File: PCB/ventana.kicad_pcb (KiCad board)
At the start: 2 copper layers, 78 x 49 mm, 55 parts, among them J1 Prog, J10 CLS, J2 SW1, J3 GND, J4 SW2, J5 GND, J6 VBat, J7 Motor+, J8 Motor-, J9 GND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

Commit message: Schematic and PCB
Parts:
- added C10: .01, Capacitor_SMD:C_1206_3216Metric, F.Cu at (105.8, 68.5)
- added C11: .01, Capacitor_SMD:C_1206_3216Metric, F.Cu at (105.8, 71.7)
- added D6: BZV55-B5V1.115, Diode_SMD:D_SOD-123, F.Cu at (100.2, 68.5)
- added D7: BZV55-B5V1.115, Diode_SMD:D_SOD-123, F.Cu at (100.2, 71.8)
- added R22: R, Resistor_SMD:R_1206_3216Metric, F.Cu at (111.5, 68.5)
- added R23: R, Resistor_SMD:R_1206_3216Metric, F.Cu at (111.5, 71.7)
- R21: value R47 -> 470

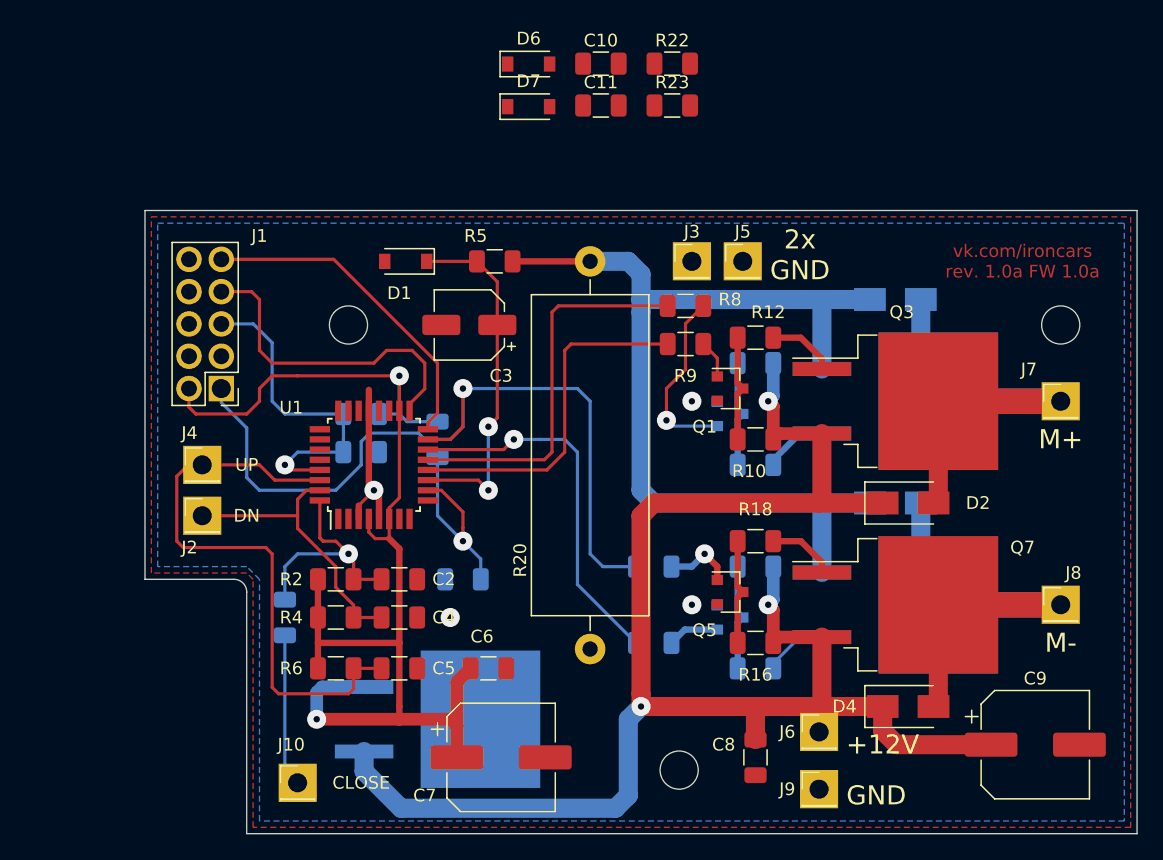
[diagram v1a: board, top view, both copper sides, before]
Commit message: Added parts for midpoints voltage measurement
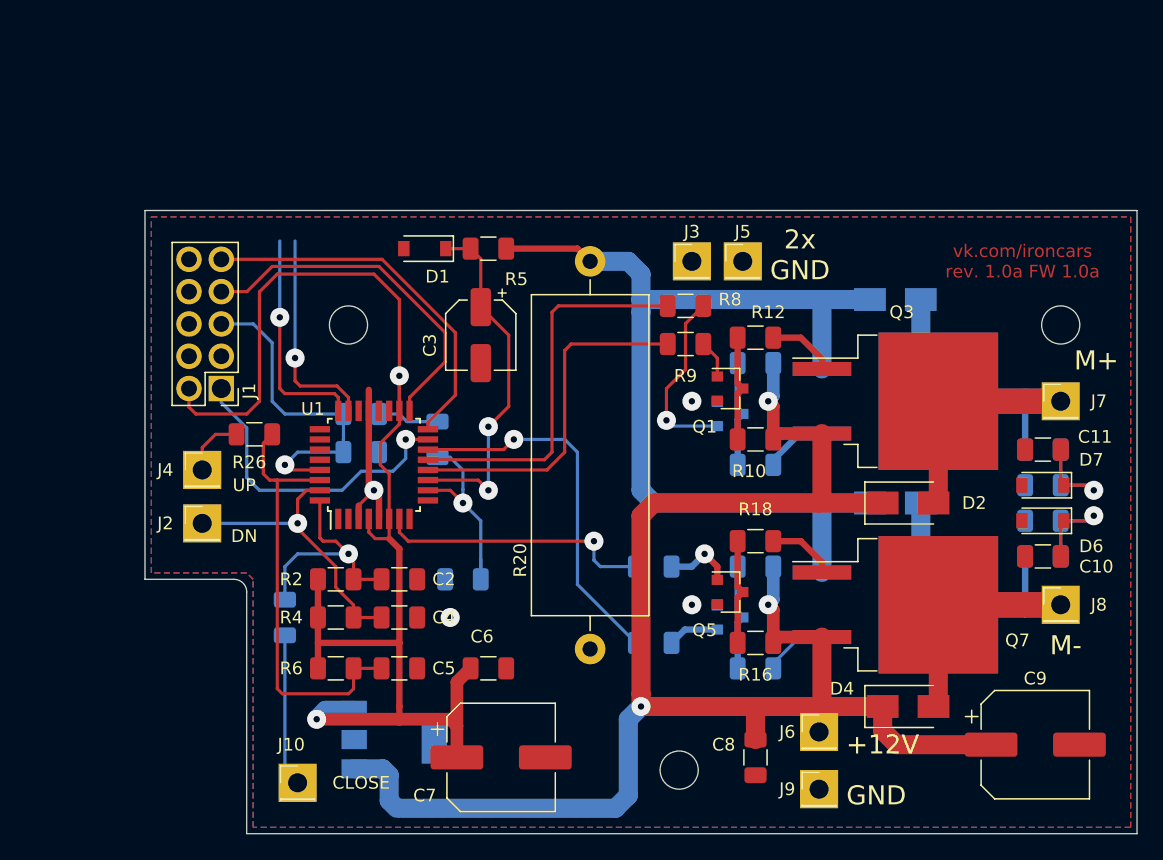
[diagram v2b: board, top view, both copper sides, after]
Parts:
- added R24: R, Resistor_SMD:R_1206_3216Metric, B.Cu at (140.6, 101.6)
- added R25: R, Resistor_SMD:R_1206_3216Metric, B.Cu at (140.6, 104.4)
- added R26: R, Resistor_SMD:R_1206_3216Metric, F.Cu at (78.6, 97.6)
- R22, R23: moved to B.Cu
- U2: value LM7805 -> LM2937; footprint Package_TO_SOT_SMD:TO-263-2 -> Package_TO_SOT_SMD:SOT-223
- moved D6 54.1 mm to (140.6, 104.4), turned to 180 degrees
- moved C10 52.0 mm to (140.6, 107.2)
- moved D7 50.2 mm to (140.6, 101.6), turned to 180 degrees
- moved R23 45.9 mm to (140.6, 107.2)
- moved C11 44.0 mm to (140.6, 98.8)
- moved R22 42.1 mm to (140.6, 98.8)
- moved U2 3.76 mm to (89.6, 121.6)
- moved D1 1.80 mm to (92.0, 83.0)
- moved C3 1.20 mm to (96.4, 89.8), turned to 270 degrees
- moved R5 1.12 mm to (97.0, 83.0)
- moved J2 0.60 mm to (74.5, 104.6)
- moved J4 0.40 mm to (74.5, 100.4)
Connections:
- J4 pad 1: Net-(C5-Pad1) -> Net-(J4-Pad1)
- R15 pad 2: Net-(J1-Pad1) -> Net-(R15-Pad2)
- R23 pad 1: Net-(D2-Pad2) -> Net-(D4-Pad2)
- U1 pad 7: Net-(U1-Pad7) -> Net-(R15-Pad2)
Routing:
- net Net-(J1-Pad1): track 64.4 -> 25.0 mm
- net Net-(C10-Pad2): track 0.00 -> 28.5 mm, vias 0 -> 2
- net Net-(C11-Pad2): track 0.00 -> 27.8 mm, vias 0 -> 2
- net Net-(R15-Pad2): track 0.00 -> 21.6 mm, vias 0 -> 1
- net Net-(C6-Pad1): track 96.5 -> 108.9 mm
- net Net-(C5-Pad1): track 46.2 -> 34.6 mm
- net Net-(J4-Pad1): track 0.00 -> 4.88 mm
- net Net-(D4-Pad2): track 36.0 -> 39.8 mm
- net Net-(D2-Pad2): track 36.0 -> 39.8 mm
- net Net-(J1-Pad9): track 25.9 -> 29.3 mm
- net Net-(J1-Pad7): track 25.7 -> 28.4 mm
- net Net-(D3-Pad2): track 76.9 -> 77.8 mm
- net Net-(C4-Pad1): vias 0 -> 1

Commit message: PCB rev 1.0b
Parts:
- added G***: LOGO, Ventana:buho_10mm, F.Cu at (133.0, 83.0)
- added R27: R, Resistor_SMD:R_1206_3216Metric, F.Cu at (80.4, 104.0)
- moved J3 9.06 mm to (122.0, 83.0)
- moved J6 8.61 mm to (130.4, 125.4)
- moved J5 4.12 mm to (113.0, 83.0)
- moved J9 1.00 mm to (122.0, 125.6)
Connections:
- J2 pad 1: Net-(C4-Pad1) -> Net-(J2-Pad1)
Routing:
- net Net-(C10-Pad2): track 28.5 -> 124.8 mm
- net Net-(C11-Pad2): track 27.8 -> 118.4 mm
- net Net-(C4-Pad1): track 24.0 -> 15.4 mm, vias 1 -> 0
- net Net-(J2-Pad1): track 0.00 -> 5.85 mm
- net +12V: track 133.2 -> 131.9 mm
- net GND: vias 4 -> 7
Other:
- board size 78 x 49 mm -> 78 x 54 mm
- board text added: "vk.com/ironcars rev. 1.0b"
- board text added: "Контроллер стеклоподъёмника"
- board text removed: "2x GND"
- board text removed: "vk.com/ironcars rev. 1.0a FW 1.0a"
